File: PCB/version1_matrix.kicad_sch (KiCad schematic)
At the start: 184 parts

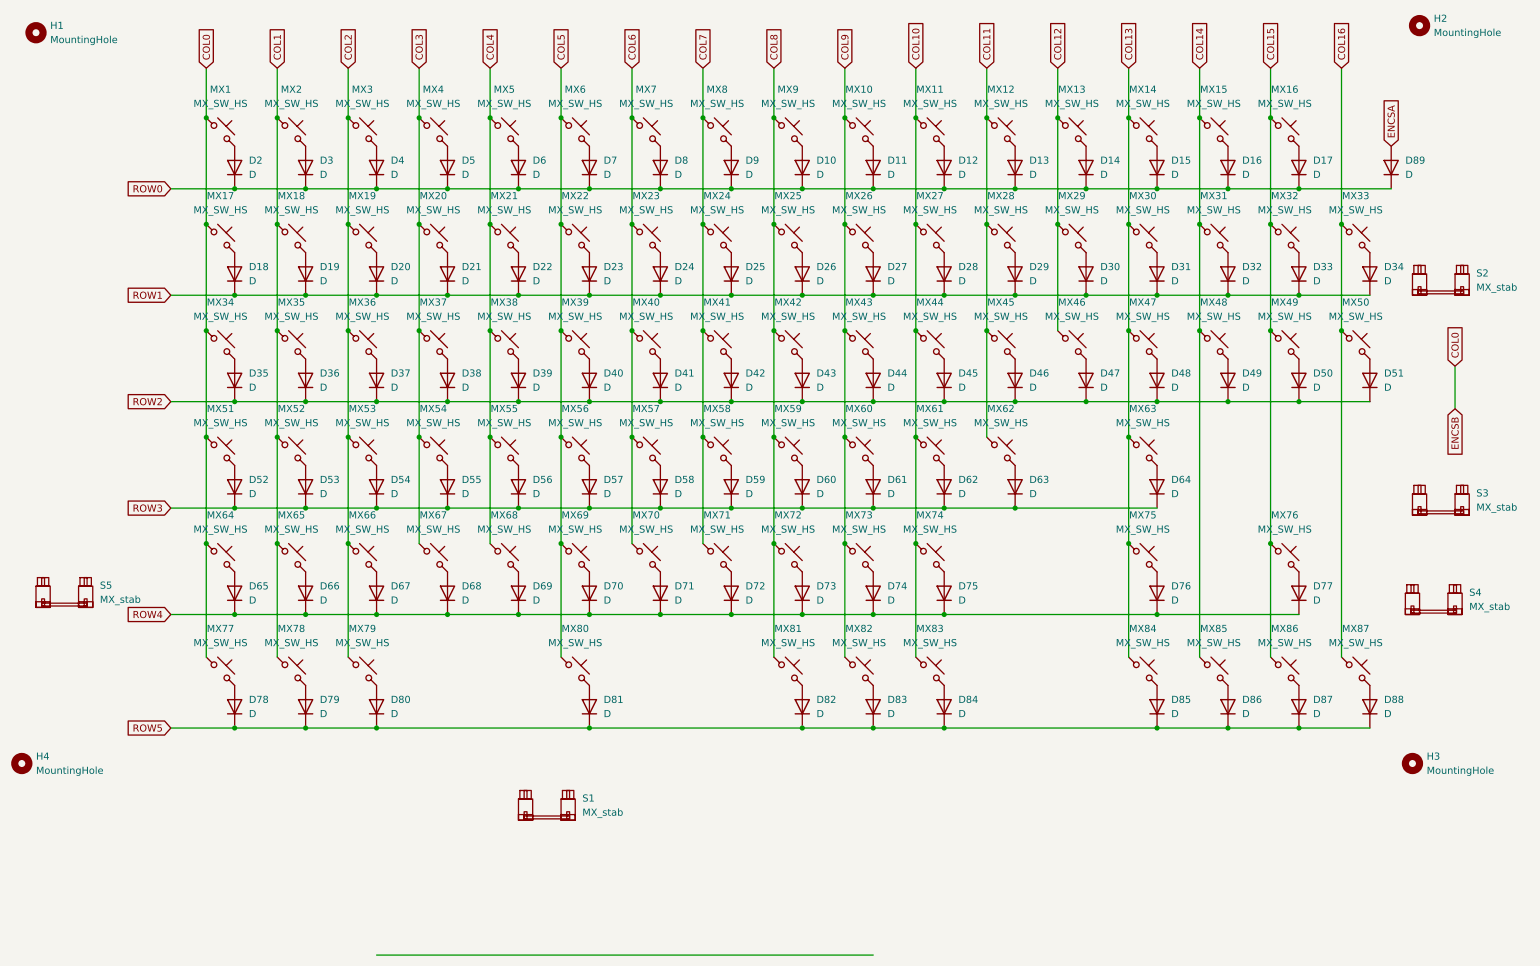
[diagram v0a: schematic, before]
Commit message: Updated PCB, gerbers and added STEP files to production folder
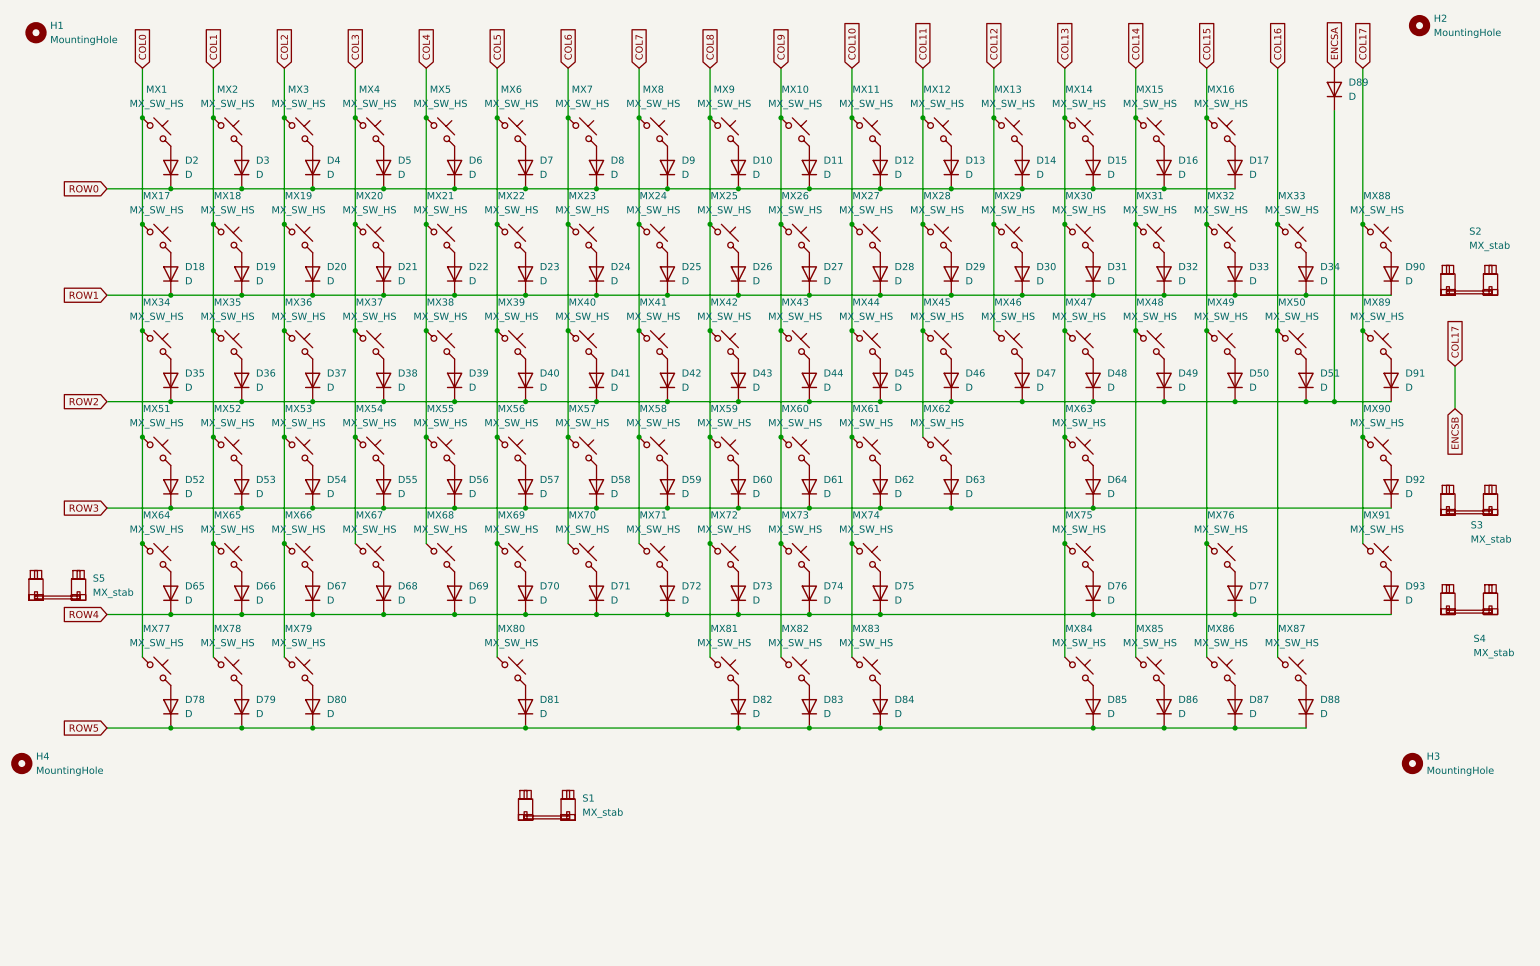
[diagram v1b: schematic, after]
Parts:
- added D90, D91, D92, D93: D, Diode_SMD:D_SOD-123, symbol Device:D
- added MX88, MX89, MX90, MX91: MX_SW_HS, PCM_marbastlib-mx:SW_MX_HS_CPG151101S11_1u, symbol PCM_marbastlib-mx:MX_SW_HS_CPG151101S11
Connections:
- net ROW0: no longer D89.1 (K)
- net ROW1: now also D90.1 (K)
- net ROW2: now also D89.1 (K), D91.1 (K)
- net ROW3: now also D92.1 (K)
- net ROW4: now also D93.1 (K)
- new net: D91.2 (A), MX89.2
- new net: D90.2 (A), MX88.2
- new net: D93.2 (A), MX91.2
- new net: D92.2 (A), MX90.2
- new net COL17: MX88.1, MX89.1, MX90.1, MX91.1
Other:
- moved on the sheet: D10, D11, D12, D13, D14, D15, D16, D17, D18, D19, D2, D20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
